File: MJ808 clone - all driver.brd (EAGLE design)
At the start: 22 x 22 mm, 30 parts, among them IC1 MAX16820, IC3 MCP2515, IC4 ATTINY4313-MMH, IC5 MCP2561-2, IC8 PRQV8.00CR1510Y00L, IC9 TPS709-Q1, Q11 PMV213SN,215

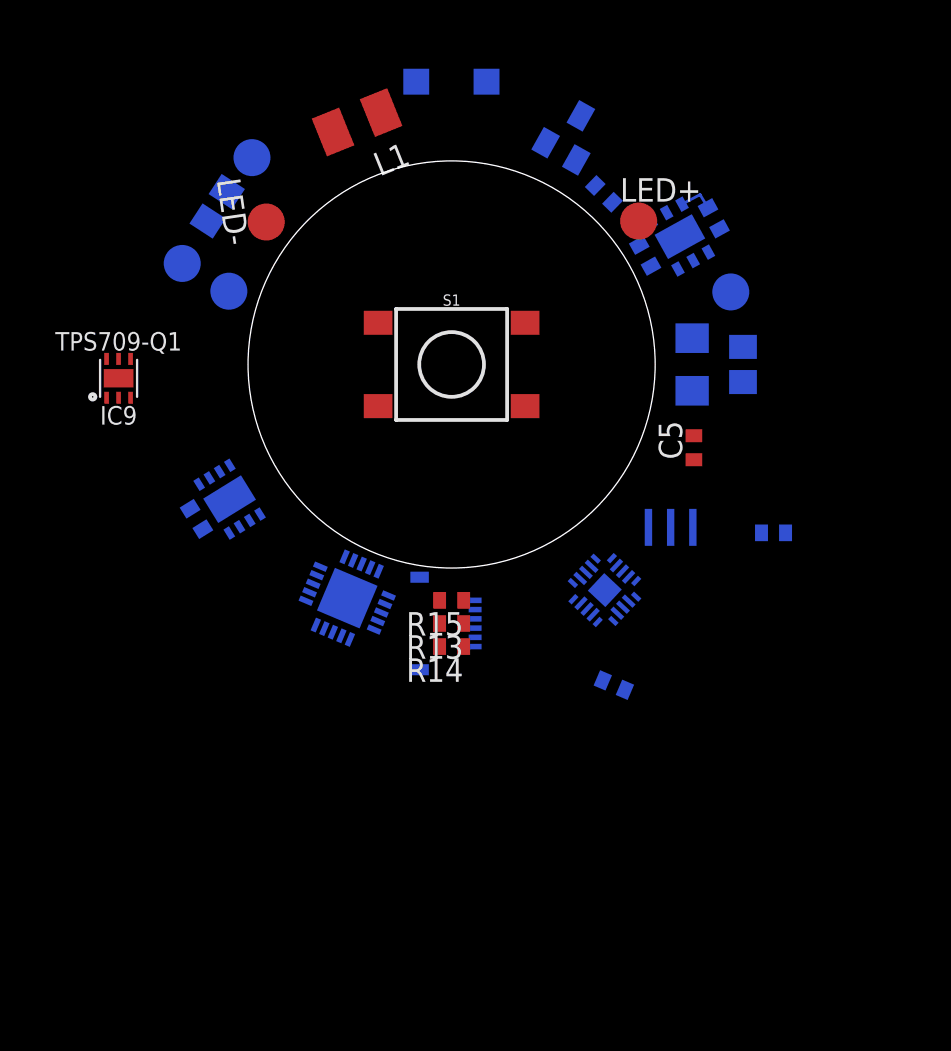
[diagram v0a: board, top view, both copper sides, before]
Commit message: - added master switch - unlocked elements on final board
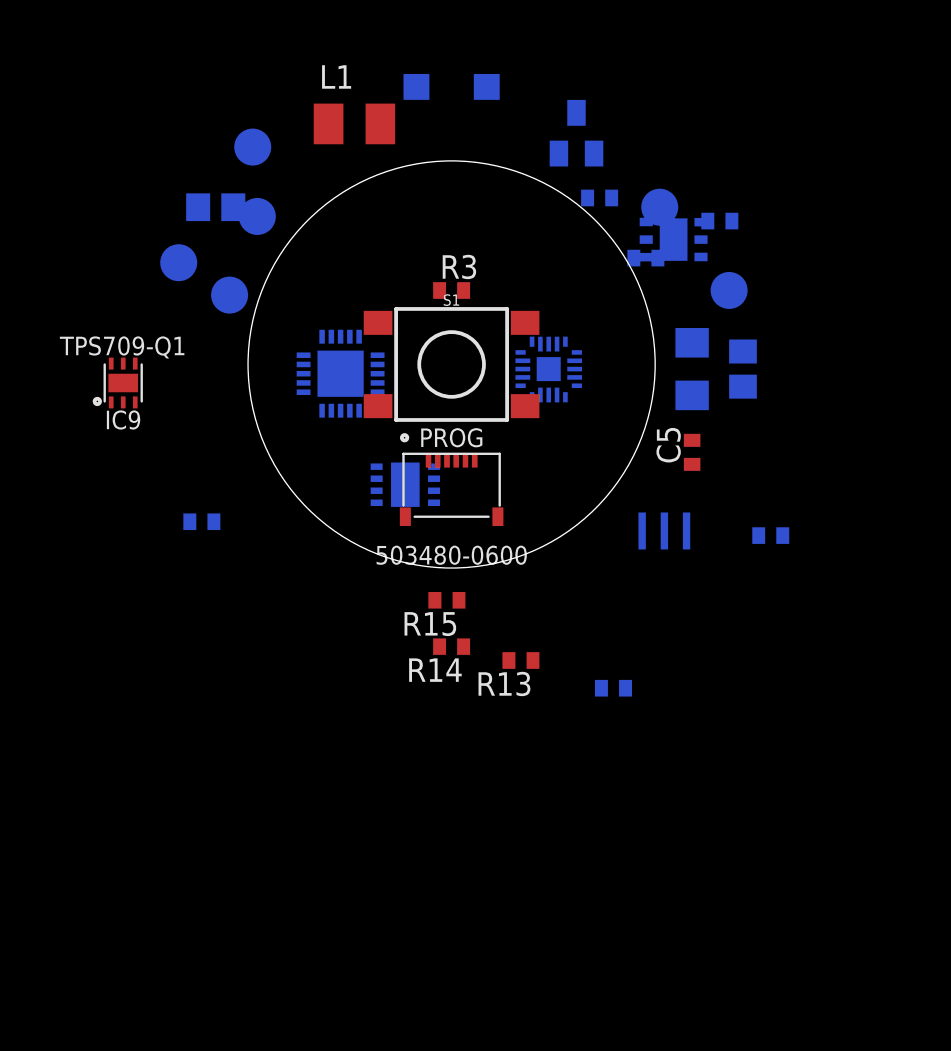
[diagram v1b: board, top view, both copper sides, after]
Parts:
- added R3: 10k, rcl:R0402
- moved IC4 12.3 mm to (5.25, -0.25), turned to 180 degrees
- moved IC3 12.1 mm to (-6.00, -0.50), turned to 180 degrees
- moved IC5 9.53 mm to (-2.50, -6.50), turned to 90 degrees
- moved PROG 7.50 mm to (0.00, -6.50), flipped to the top, turned to 0 degrees
- moved R13 4.25 mm to (3.75, -16.0)
- moved LED+ 1.36 mm to (11.2, 8.50), flipped to the bottom
- moved CANH 0.57 mm to (-10.8, 11.8)
- moved LED- 0.57 mm to (-10.5, 8.00), flipped to the bottom, turned to 188.3 degrees
- moved IC8 0.39 mm to (11.5, -9.00)
- moved IC1 0.38 mm to (12.0, 6.75), turned to 0 degrees
- moved C8 0.36 mm to (14.5, 7.75), turned to 0 degrees
- moved IC9 0.35 mm to (-17.8, -1.00)
- moved C3 0.33 mm to (-13.5, -8.50), turned to 0 degrees
- moved R7 0.32 mm to (8.00, 9.00), turned to 0 degrees
- moved Q11 0.30 mm to (6.75, 12.5), turned to 0 degrees
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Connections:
- new net SWITCH: IC4.PB3, R3.2, S1.B2
- net 5V0: now also S1.A2
- net GND: now also R3.1
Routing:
- net 5V0: track 1.93 -> 0.00 mm

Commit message: - updated CAM job, redo of gerbers
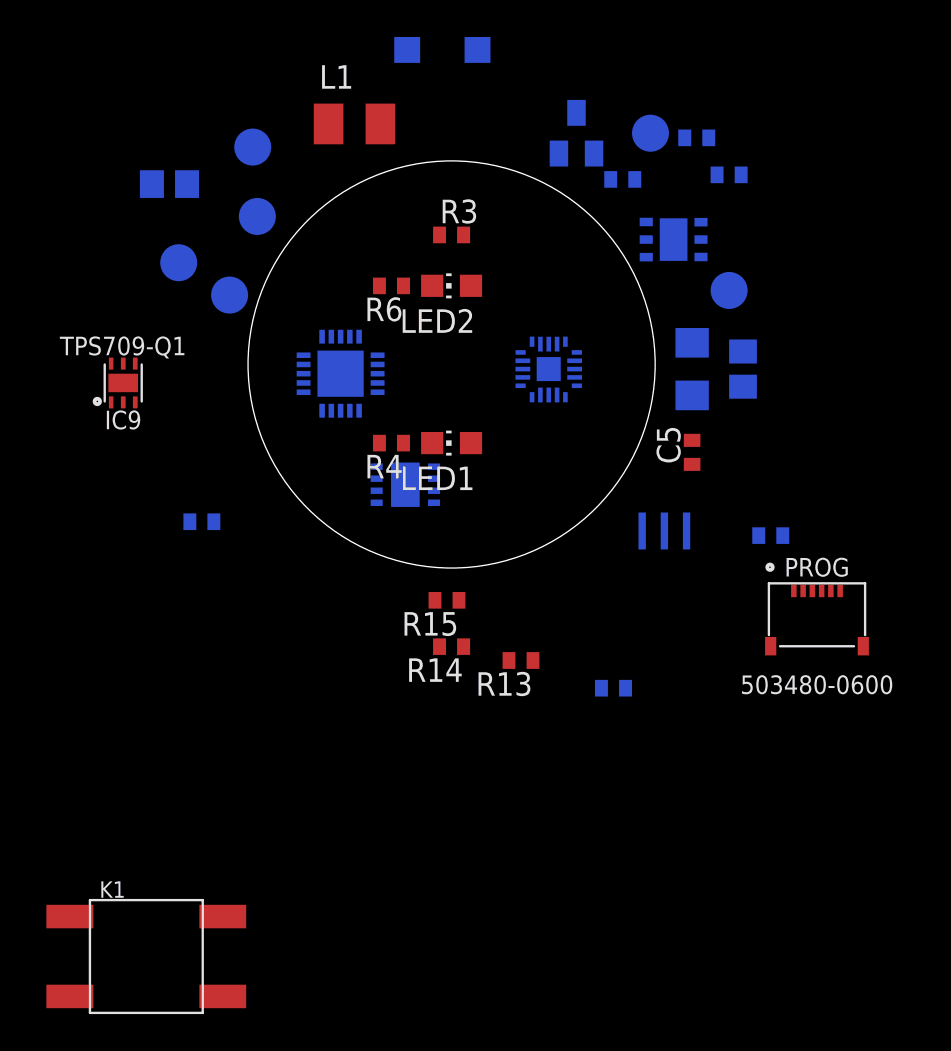
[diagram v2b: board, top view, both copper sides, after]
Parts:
- removed S1: MOMENTARY-SWITCH-SPST-SMD-6.2MM-TALL, SparkFun-Switches:TACTILE_SWITCH_SMD_6.2MM_TALL
- added K1: (no value), Seeed-Switch:SW4-SMD-6.0X6.0X5.0MM
- added LED1, LED2: (no value), led:CHIP-LED0805
- added R4, R6: 330, rcl:R0402
- moved PROG 21.0 mm to (19.8, -13.5)
- moved R1 7.06 mm to (13.2, 12.2)
- moved LED+ 4.03 mm to (10.8, 12.5)
- moved R3 3.00 mm to (0.00, 7.00)
- moved R5 2.80 mm to (-15.2, 9.75)
- moved C8 2.55 mm to (15.0, 10.2)
- moved D1 2.06 mm to (-0.50, 17.0)
- moved R7 1.60 mm to (9.25, 10.0)
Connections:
- new net LED1: IC4.PB2, R4.2
- new net LED2: IC4.PB1, R6.2
- new net N$11: LED2.C, R6.1
- new net N$12: LED1.C, R4.1
- net 5V0: now also K1.3, LED1.A, LED2.A; no longer S1.A2
- net STBY: now also IC4.PB0; no longer IC4.PB1
- net SWITCH: now also K1.4; no longer S1.B2
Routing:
- net SPI_SS: track 21.9 -> 0.00 mm
- net DIM_FRONT: track 14.0 -> 0.00 mm
- net DIM_BRAKE_DRAIN: track 10.4 -> 0.00 mm
- net TXCAN: track 2.55 -> 0.00 mm

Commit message: - redraw of POC board according to 1st rev of prod board, ERC & DRC check out error free, updated gerbers
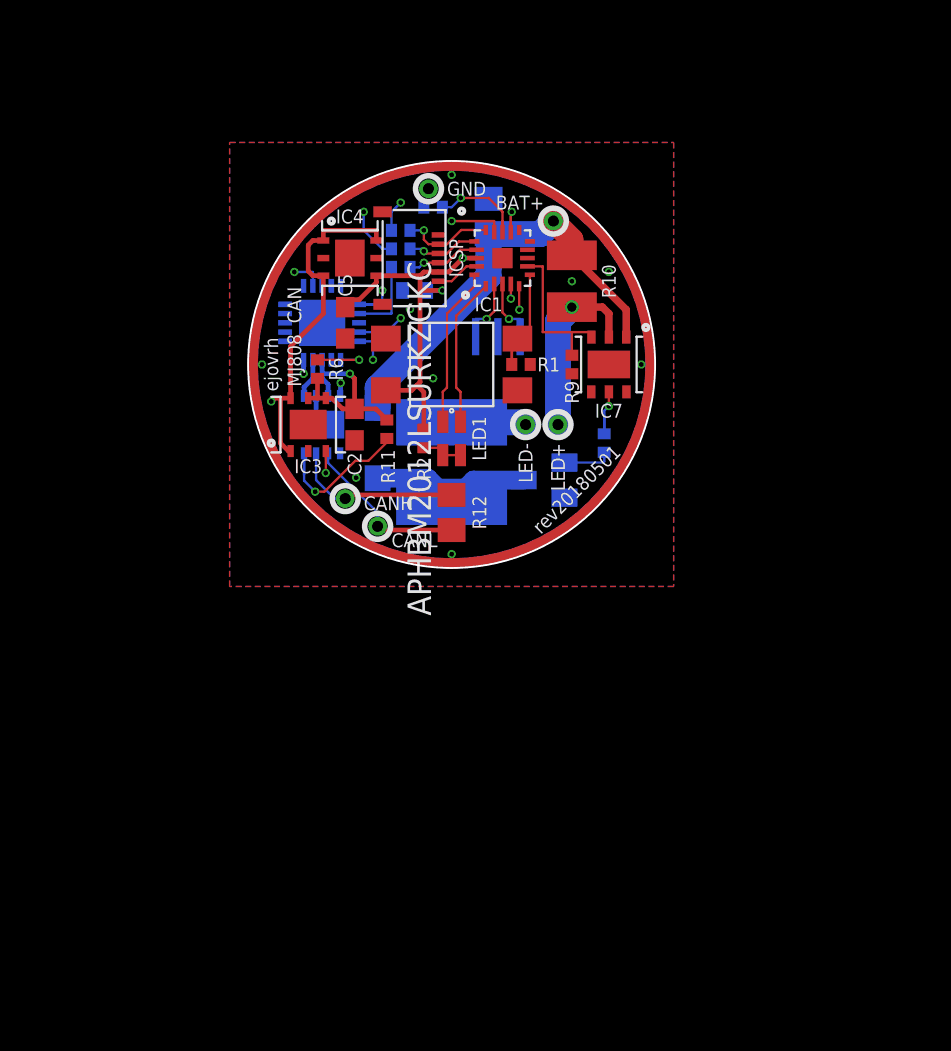
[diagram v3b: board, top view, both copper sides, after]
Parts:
- removed C3: 0.1μF, rcl:C0402
- removed C8: 1μF, rcl:C0402
- removed IC8: PRQV8.00CR1510Y00L, PRQV8.00CR1510Y00L - 8MHz resonator:SMT
- removed IC9: TPS709-Q1, TPS709-q1 5V LDO:WSON6
- removed K1: (no value), Seeed-Switch:SW4-SMD-6.0X6.0X5.0MM
- removed LED2: (no value), led:CHIP-LED0805
- removed PROG: 503480-0600, 5034800600 FPC Connector:SMT
- removed Q11: PMV213SN,215, adafruit:SOT23
- removed R13, R14, R15: 330, rcl:R0402
- removed VBAT: TPTP20R, testpad:TP20R
- added BAT+: LiIon + Terminal, signal testpoint:TH
- added C2: 22μF, rcl:C0603
- added IC2: PRQV8.00CR1510Y00L, PRQV8.00CR1510Y00L - 8MHz resonator:SMT
- added IC6: MCP2561-2, MCP2561-2 - High-Speed CAN Transceiver:DFN10
- added IC7: MAX16820, MAX16820 LED Driver, constant current:TDFN-6-EP
- added ICSP: 5034800600, 5034800600 FPC Connector:SMT
- added Q1: PMV213SN,215, adafruit:SOT23
- added R10: 0.15 / 1W, rcl:R1210
- added R11, R9: 10k, rcl:R0402
- added R12: 120, rcl:R0805
- added SW1: TL3305-844809, TL3305-844809 SPST-NO Tact Switch:SMD
- C1: value 47μF / 15V+ -> 0.1μF; device rcl:C0805 -> rcl:C0402
- C4: value 0.1μF -> 47μF / 15V+; device rcl:C0402 -> rcl:C0805
- C5: value 0.1μF -> 22μF; device rcl:C0402 -> rcl:C0603
- CANH: value TPTP20R -> CAN high; device testpad:TP20R -> signal testpoint:TH
- CANL: value TPTP20R -> CAN low; device testpad:TP20R -> signal testpoint:TH
- GND: value TPTP20R -> LiIon - Terminal; device testpad:TP20R -> signal testpoint:TH
- IC1: value MAX16820 -> ATTINY4313-MMH; device MAX16820 LED Driver, constant current:TDFN-6-EP -> ATtiny4313 microcontroller:VQFN-20
- IC3: value MCP2515 -> LP38693SD-5.0/NOPB; device MCP2515-I-ML - Standalonce CAN Controller with SPI Interface:QFN20 -> LP38693 5V LDO:WSON6
- IC4: value ATTINY4313-MMH -> LP38693SD-5.0/NOPB; device ATtiny4313 microcontroller:VQFN-20 -> LP38693 5V LDO:WSON6
- IC5: value MCP2561-2 -> MCP2515; device MCP2561-2 - High-Speed CAN Transceiver:DFN10 -> MCP2515-I-ML - Standalonce CAN Controller with SPI Interface:QFN20
- L1: value AISC-1210HS-330K-T2 -> VLS6045EX-150M-CA; device eagle-ltspice:L3225M -> SparkFun-Coils:SRN6045
- LED+: value TPTP20R -> LED anode; device testpad:TP20R -> signal testpoint:TH
- LED-: value TPTP20R -> LED cathode; device testpad:TP20R -> signal testpoint:TH
- LED1: value (none) -> APHBM2012LSURKZGKC; device led:CHIP-LED0805 -> APHBM2012LSURKZGKC:SMD
- R2: value 0.25 / 0.25W -> 10k; device rcl:R1206 -> rcl:R0402
- R5: value 120 -> 330; device rcl:R0805 -> rcl:R0402
- R6: value 330 -> 10k
- R7: value 10k -> 330
- moved C4 23.0 mm to (2.00, 8.00), turned to 90 degrees
- moved D1 21.5 mm to (-4.00, -4.25), turned to 270 degrees
- moved C5 20.0 mm to (-5.75, 2.25)
- moved CANH 19.6 mm to (-5.75, -7.25), flipped to the top
- moved L1 19.0 mm to (0.00, -5.25), flipped to the bottom, turned to 90 degrees
- moved LED- 18.4 mm to (4.00, -3.25), flipped to the top, turned to 0 degrees
- moved C1 18.3 mm to (-2.00, 4.00), turned to 0 degrees
- moved CANL 17.9 mm to (-4.00, -8.75), flipped to the top
- moved LED+ 16.5 mm to (5.75, -3.25), flipped to the top
- moved R1 15.5 mm to (3.75, 0.00), flipped to the top
- moved R2 15.0 mm to (-1.50, -4.00), flipped to the top
- moved R8 13.3 mm to (8.25, -4.25), turned to 270 degrees
- moved R5 12.7 mm to (-2.75, 7.25), turned to 180 degrees
- moved R7 12.6 mm to (-2.75, 6.25), turned to 180 degrees
- moved IC4 12.3 mm to (-5.50, 5.75), flipped to the top, turned to 270 degrees
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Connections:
- removed net 5V0: C4.1, C8.1, IC1.VCC, IC4.VCC, K1.3, LED1.A, LED2.A
- removed net 5V0_REG: C3.1, C5.1, IC3.VDD, IC5.VDD, IC9.OUT, R8.1
- removed net CKOUT: IC3.OSC1, IC4.PD2
- removed net CSN: IC1.CSN, LED+.TP, R2.1
- removed net DEBUGWIRE: IC4.PA2
- removed net INT1: IC3.!INT!, IC4.PD3
- removed net LED1: IC4.PB2, R4.2
- removed net LED2: IC4.PB1, R6.2
- removed net N$1: PROG.GND1, PROG.GND2
- removed net N$11: LED2.C, R6.1
- removed net N$12: LED1.C, R4.1
- removed net N$2: PROG.6
- removed net N$3: L1.2, LED-.TP
- removed net N$4: PROG.5
- removed net N$5: PROG.4
- removed net N$6: PROG.3
- removed net N$7: PROG.2
- removed net N$8: PROG.1
- removed net SCK: IC4.PB7, R15.1
- removed net SI: IC4.PB5, R13.1
- removed net SO: IC4.PB6, R14.1
- removed net VBAT: C1.1, D1.C, IC1.IN, IC9.IN, R2.2, VBAT.TP
- new net 5V0_CAN: C2.1, IC3.4-OUT, IC3.5-SNS, IC5.VDD, IC6.VDD, R11.1, R6.1
- new net 5V0_μC: C1.1, C5.2, IC1.VCC, IC4.4-OUT, ICSP.5, R2.2, SW1.1, SW1.2
- new net BAT+: BAT+.TP$1, C4.1, D1.C, IC3.1-IN, IC3.6-IN, IC4.1-IN, IC4.3-EN, IC4.6-IN, IC7.IN, R10.2
- new net CLOCKOUT: IC1.PD2, IC5.OSC1
- new net DEBUGWIRE/RESET: IC1.PA2, ICSP.6
- new net GREEN_LED: IC1.PD0, LED1.3
- new net ICSP_MISO: IC1.PB6, ICSP.3, R7.2
- new net ICSP_MOSI: IC1.PB5, ICSP.2, R5.2
- new net ICSP_SCK: IC1.PB7, ICSP.4, R4.2
- new net INT: IC1.PD3, IC5.!INT!
- new net LED: LED1.1, LED1.4, R2.1
- new net LED_AN: IC7.CSN, LED+.TP$1, R10.1
- new net LED_CA: L1.2, LED-.TP$1
- new net RED_LED: IC1.PD1, LED1.2
- new net VCC: IC7.VCC
- net CANH: now also CANH.TP$1, IC6.CANH, R12.2; no longer CANH.TP, IC5.CANH, R5.2
- net CANL: now also CANL.TP$1, IC6.CANL, R12.1; no longer CANL.TP, IC5.CANL, R5.1
- net DIM_BRAKE_DRAIN: now also Q1.3; no longer Q11.3
- net DIM_FRONT: now also IC1.PD5, IC7.DIM, R9.1; no longer IC1.DIM, IC4.PD5, R1.2
- net DIM_FRONT_GATE: now also IC7.DRV, R8.1; no longer IC1.DRV, R7.1
- net EN: now also IC1.PB3, IC3.3-EN, R3.2; no longer IC9.EN
- net GATE: now also Q1.1, R8.2; no longer Q11.1, R7.2
- net GND: now also C2.2, C5.1, GND.TP$1, IC2.GND, IC3.2-GND, IC4.2-GND, IC5.GND6, IC6.GND, IC6.VSS, IC7.GND, IC7.GND1, ICSP.1, ICSP.GND1, ICSP.GND2, Q1.2, R1.2, R9.2; no longer C3.2, C5.2, C8.2, GND.TP, IC3.GND, IC3.GND6, IC4.GND, IC5.VSS, IC8.GND, IC9.GND, IC9.GND1, Q11.2, R1.1
- net RXCAN: now also IC5.RXCAN, IC6.RXD; no longer IC3.RXCAN, IC5.RXD
- net SPI_MISO: now also IC5.SO, R7.1; no longer IC3.SO, R14.2
- net SPI_MOSI: now also IC5.SI, R5.1; no longer IC3.SI, R13.2
- net SPI_SCK: now also IC5.SCK, R4.1; no longer IC3.SCK, R15.2
- net SPI_SS: now also IC1.PB4, IC5.!CS!, R6.2; no longer IC3.!CS!, IC4.PB4, R8.2
- net STBY: now also IC1.PB2, IC6.STBY, R11.2; no longer IC4.PB0, IC5.STBY
- net SWITCH: now also IC1.PD4, R1.1, SW1.3, SW1.4; no longer IC4.PB3, K1.4, R3.2
- net TXCAN: now also IC5.TXCAN, IC6.TXD; no longer IC3.TXCAN, IC5.TXD
- net XTAL1: now also IC1.PA0, IC2.XTAL1; no longer IC4.PA0, IC8.XTAL1
- net XTAL2: now also IC1.PA1, IC2.XTAL2; no longer IC4.PA1, IC8.XTAL2
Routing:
- net GND: track 0.00 -> 88.7 mm, vias 0 -> 9
- net BAT+: track 0.00 -> 67.1 mm, vias 0 -> 1
- net STBY: track 0.00 -> 30.5 mm, vias 0 -> 2
- net EN: track 0.00 -> 25.0 mm, vias 0 -> 2
- net 5V0_μC: track 0.00 -> 20.8 mm, vias 0 -> 2
- net SPI_SS: track 0.00 -> 17.0 mm, vias 0 -> 2
- net CLOCKOUT: track 0.00 -> 14.8 mm, vias 0 -> 2
- net SPI_MISO: track 0.00 -> 12.9 mm, vias 0 -> 2
- net 5V0_CAN: track 0.00 -> 11.9 mm, vias 0 -> 1
- net INT: track 0.00 -> 11.9 mm, vias 0 -> 2
- net SPI_MOSI: track 0.00 -> 10.5 mm, vias 0 -> 2
- net LED_AN: track 0.00 -> 10.1 mm, vias 0 -> 1
- net CANL: track 0.00 -> 9.42 mm
- net CANH: track 0.00 -> 9.27 mm
- net DIM_BRAKE_DRAIN: track 0.00 -> 9.06 mm
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- added copper zone on layer 1, net GND
- added copper zone on layer 15, net GND
- added copper zone on layer 16, net GND
- added copper zone on layer 2, net GND
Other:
- board text added: "MJ808 CAN"
- board text added: "ejovrh"
- board text added: "rev20180501"

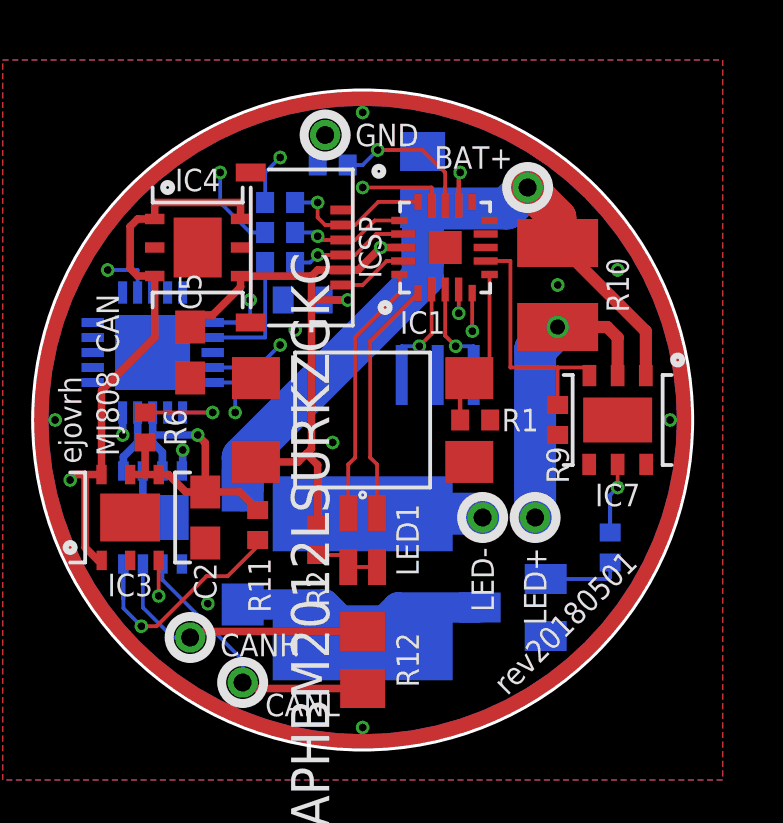
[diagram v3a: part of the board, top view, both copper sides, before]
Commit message: - moved PWN line for front light to OC1A, DRC & ERC are ok, updated gerbers
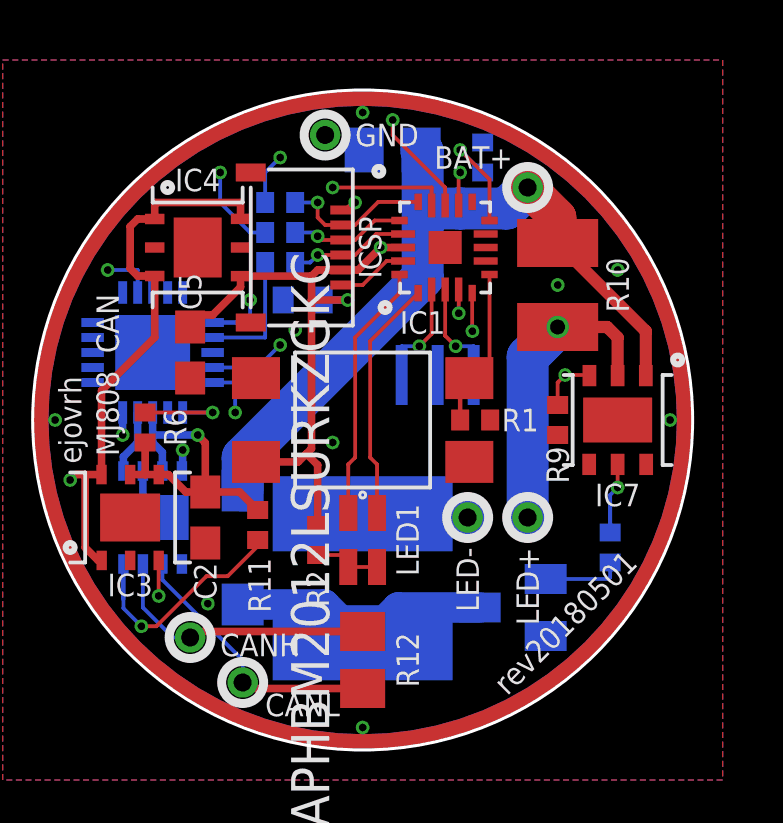
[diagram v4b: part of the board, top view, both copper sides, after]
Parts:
- moved R3 5.01 mm to (4.00, 8.75), turned to 270 degrees
- moved C4 1.41 mm to (1.00, 9.00), turned to 0 degrees
- moved LED- 0.50 mm to (3.50, -3.25)
- moved LED+ 0.25 mm to (5.50, -3.25)
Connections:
- new net N$1: IC1.PD6
- new net N$2: IC1.PD5
- new net N$3: IC1.PB1
- net DIM_FRONT: now also IC1.PB3; no longer IC1.PD5
- net EN: now also IC1.PB0; no longer IC1.PB3
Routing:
- net DIM_FRONT: track 8.49 -> 17.8 mm, vias 0 -> 2
- net LED_AN: track 10.1 -> 11.2 mm
- net BAT+: track 67.1 -> 68.2 mm
- net LED_CA: track 4.05 -> 5.05 mm
- net EN: track 25.0 -> 24.0 mm
- net STBY: track 30.5 -> 29.6 mm
- net SPI_SS: track 17.0 -> 17.6 mm
- net GND: track 88.7 -> 89.3 mm, vias 9 -> 10
